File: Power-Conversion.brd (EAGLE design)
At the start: 170.2 x 81 mm, 109 parts, among them T3 FDN340P, U1 ATMEGA328P_TQFP, U4 PCA9685, U5 FT232RLSSOP, U7 LM2678

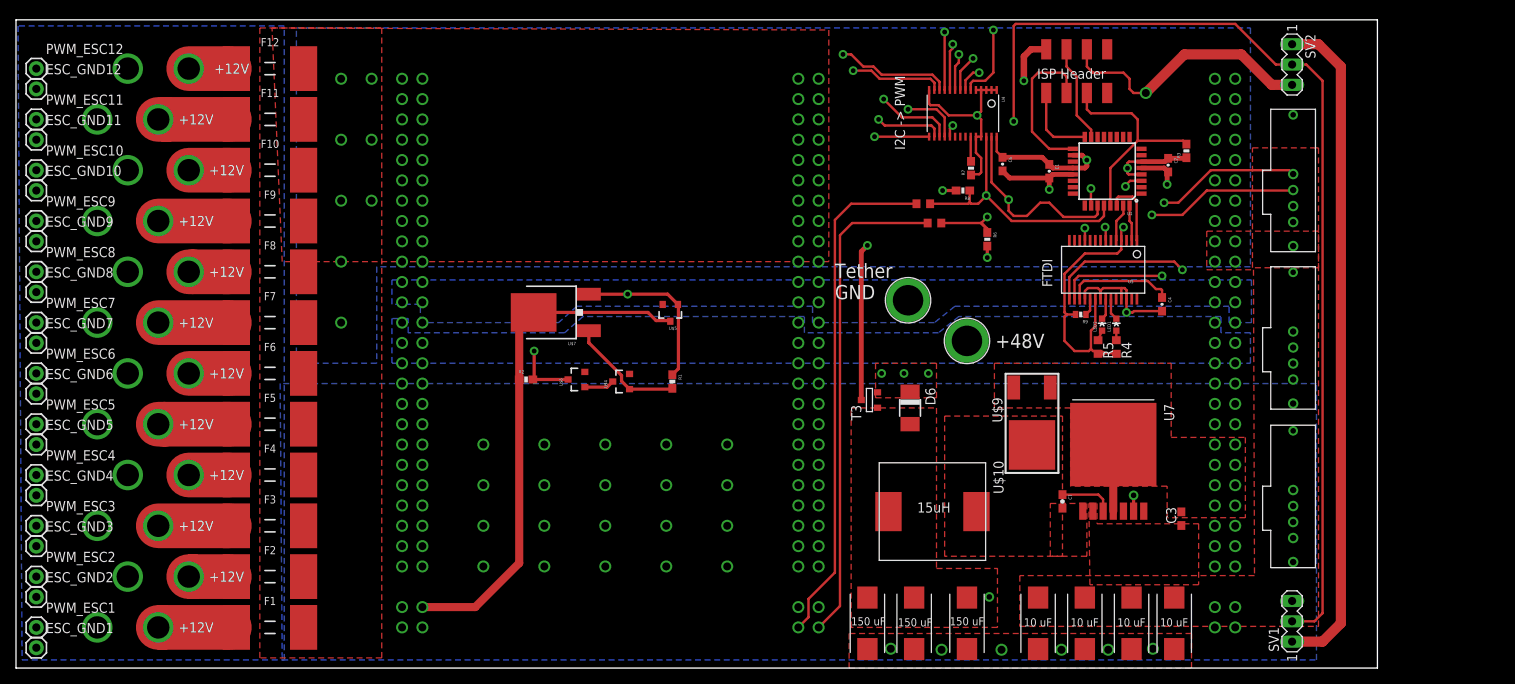
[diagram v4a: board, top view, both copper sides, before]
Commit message: Added debugging pins and more silk screen
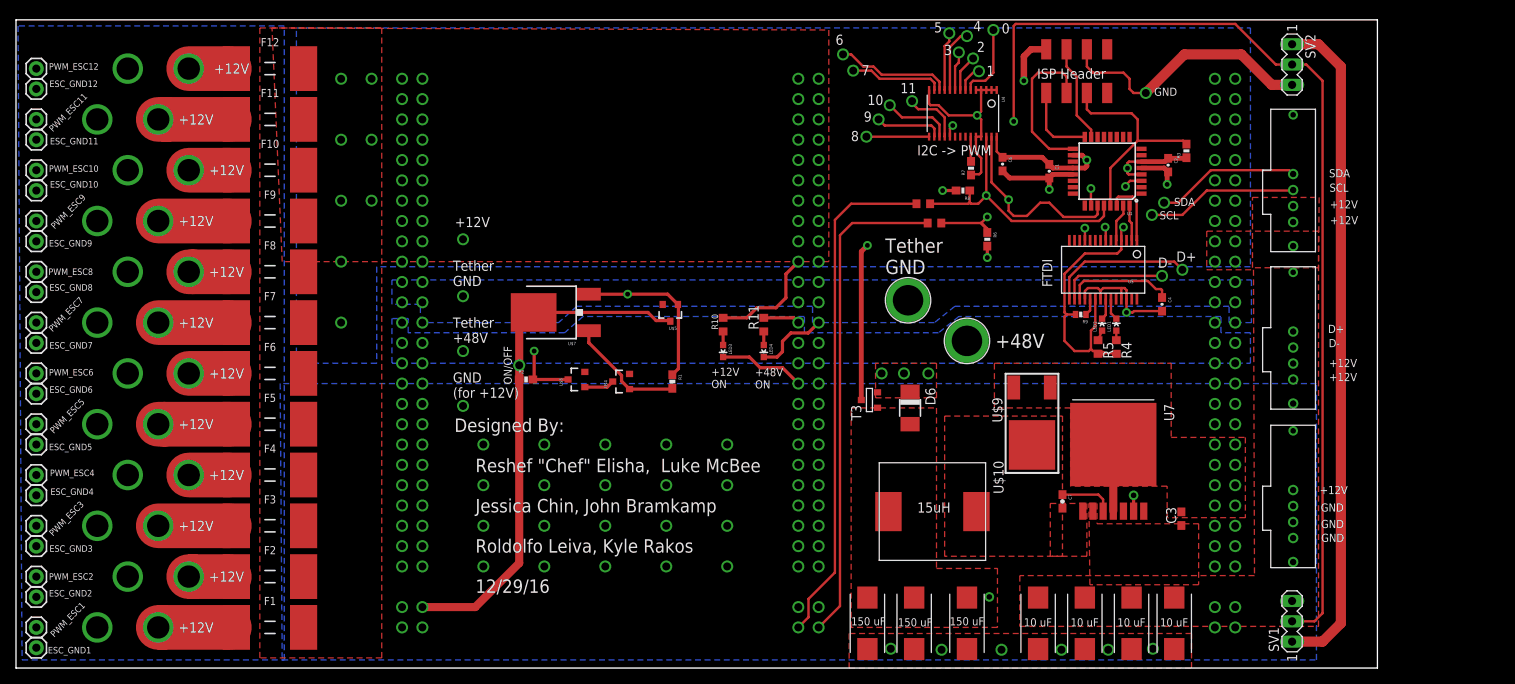
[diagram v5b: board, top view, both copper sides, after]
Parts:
- added LED3: Red, SparkFun:LED-0603
- added LED4: Green, SparkFun:LED-0603
- added R10, R11: 470, resistor:R0603
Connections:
- new net N$39: LED3.A, R10.1
- new net N$40: LED4.A, R11.1
- net GND: now also LED3.C
- net V+: now also R11.2
- net V-: now also LED4.C
- net VCC: now also R10.2
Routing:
- net VCC: track 0.00 -> 14.0 mm
- net GND: track 102.4 -> 113.2 mm
- net V-: track 20.8 -> 30.2 mm, vias 1 -> 2
- net V+: track 8.02 -> 12.6 mm, vias 1 -> 2
- net N$19: track 167.8 -> 172.0 mm
- net N$40: track 0.00 -> 1.70 mm
- net N$39: track 0.00 -> 1.70 mm
- net N$20: track 162.1 -> 162.8 mm
- net N$23: track 144.2 -> 144.8 mm
- net ONOFF: track 167.7 -> 167.9 mm, vias 0 -> 1
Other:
- board text added: "+12V ON"
- board text added: "+48V ON"
- board text added: "0"
- board text added: "1"
- board text added: "10"
- board text added: "11"
- board text added: "2"
- board text added: "3"
- board text added: "4"
- board text added: "5"
- board text added: "6"
- board text added: "7"
- board text added: "8"
- board text added: "9"
- board text added: "D+"
- board text added: "D-"
- board text added: "Designed By: Reshef "Chef" Elisha, Luke McBee Jessica Chin, John Bramkamp Roldolfo Leiva, Kyle Rakos 12/29/16"
- board text added: "GND"
- board text added: "GND (for +12V)"
- board text added: "ON/OFF"
- board text added: "SCL"
- board text added: "SDA"
- board text added: "Tether +48V"

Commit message: Fixed problem with gnd via
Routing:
- net GND: vias 33 -> 34
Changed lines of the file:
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@@
 <wire x1="93.0148" y1="37.5412" x2="95.8088" y2="37.5412" width="0.4064" layer="1"/>
 <wire x1="95.8088" y1="37.5412" x2="97.79" y2="35.56" width="0.4064" layer="1"/>
+<via x="55.88" y="32.766" extent="1-16" drill="1"/>
 </signal>
 <signal name="SCL">
@@
 <wire x1="93.472" y1="42.076" x2="93.472" y2="40.374" width="0.4064" layer="1"/>
 </signal>
-<signal name="N$41">
-<via x="55.88" y="32.766" extent="1-16" drill="1"/>
-</signal>
 <signal name="N$42">

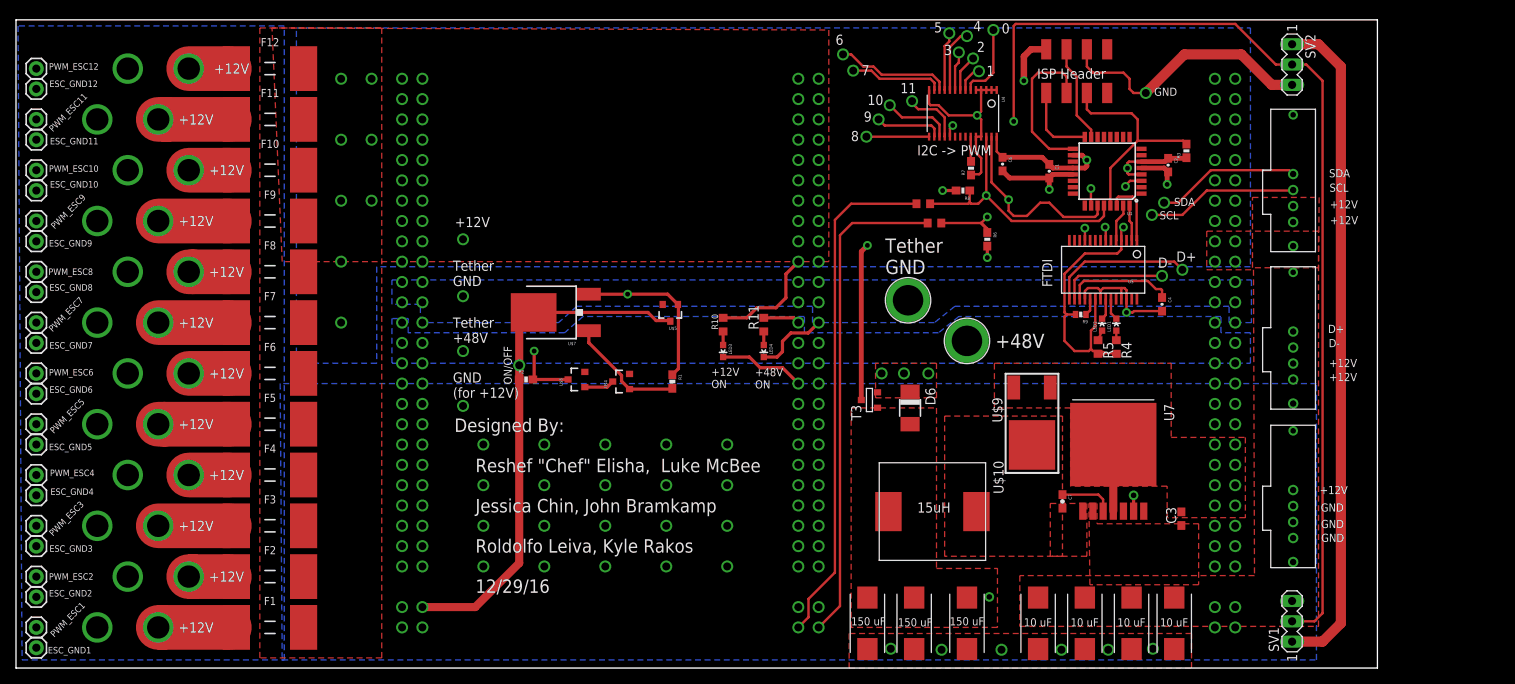
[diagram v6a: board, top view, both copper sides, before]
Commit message: Fixed a few silkscrean problems
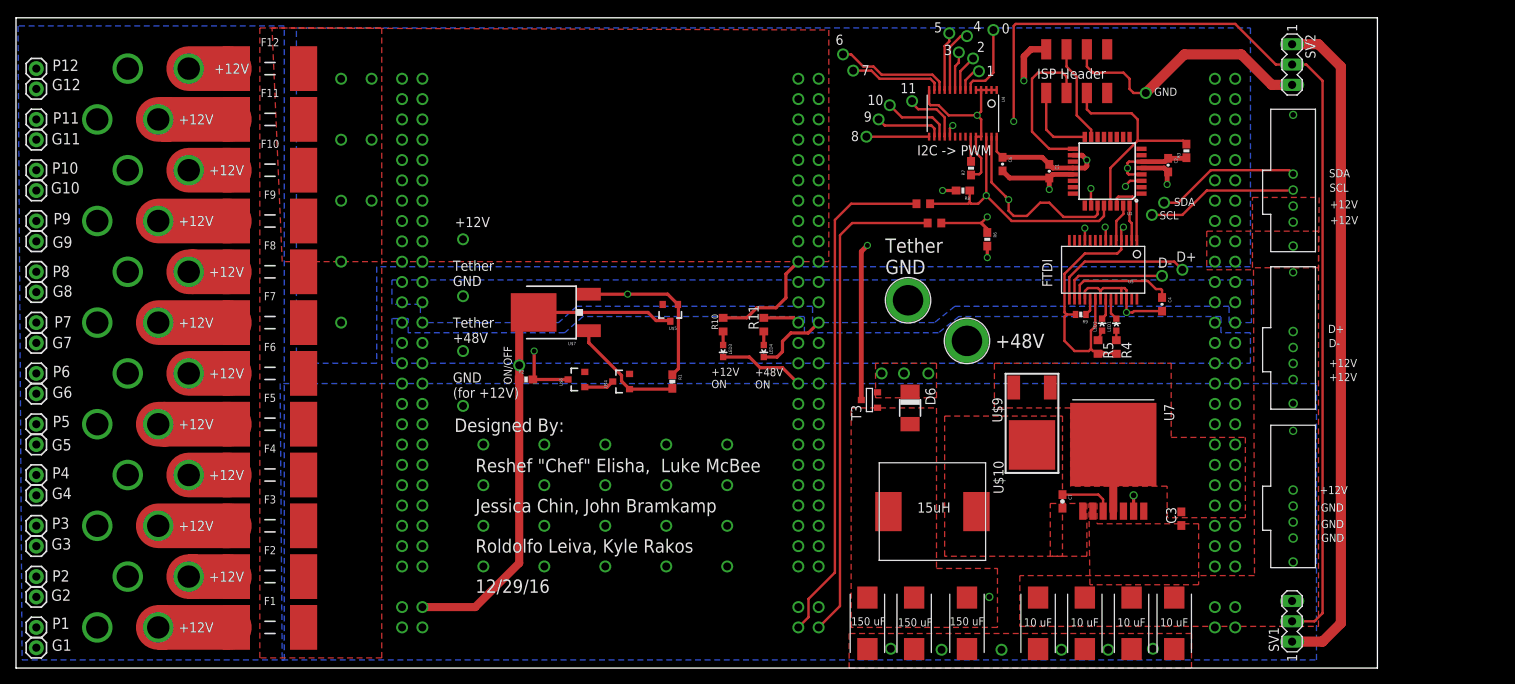
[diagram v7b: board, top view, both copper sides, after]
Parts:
- renumbered ESC_GND1 to G1, ESC_GND10 to G10, ESC_GND11 to G11, ESC_GND12 to G12, ESC_GND2 to G2, ESC_GND3 to G3, ESC_GND4 to G4, ESC_GND5 to G5, ESC_GND6 to G6, ESC_GND7 to G7, ESC_GND8 to G8, ESC_GND9 to G9, PWM_ESC1 to P1, PWM_ESC10 to P10, PWM_ESC11 to P11, PWM_ESC12 to P12, PWM_ESC2 to P2, PWM_ESC3 to P3, PWM_ESC4 to P4, PWM_ESC5 to P5, PWM_ESC6 to P6, PWM_ESC7 to P7, PWM_ESC8 to P8, PWM_ESC9 to P9
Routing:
- net VCC: vias 8 -> 9
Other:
- board size 170.2 x 81 mm -> 170.2 x 81.3 mm

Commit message: stuff
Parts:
- added LED5, LED6: Red, SparkFun:LED-0603
- added R12, R13: 470, resistor:R0603
- added RN1, RN2: (no value), resistor-dil:0603-ARC
- moved C11 1.51 mm to (127.8, 7.10)
- moved C12 1.51 mm to (139.4, 7.10)
- moved C13 1.51 mm to (133.6, 7.10)
- moved C14 1.51 mm to (144.8, 7.10)
- moved C10 1.00 mm to (118.9, 6.59)
- moved C8 1.00 mm to (106.4, 6.59)
- moved C9 1.00 mm to (112.3, 6.59)
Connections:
- new net A0: RN1.1, U4.1
- new net A1: RN1.2, U4.2
- new net A2: RN1.3, U4.3
- new net A3: RN1.4, U4.4
- new net A4: RN2.1, U4.5
- new net A5: RN2.2, U4.24
- new net LED1: R12.2, U1.1
- new net LED2: R13.2, U1.2
- new net N$41: LED5.A, R12.1
- new net N$42: LED6.A, R13.1
- net GND: now also LED5.C, LED6.C, RN1.5, RN1.6, RN1.7, RN1.8, RN2.5, RN2.6, RN2.7, RN2.8; no longer U4.1, U4.2, U4.24, U4.3, U4.4, U4.5
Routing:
- net GND: track 113.2 -> 126.4 mm, vias 34 -> 35
- net A5: track 0.00 -> 9.74 mm
- net LED1: track 0.00 -> 8.71 mm
- net LED2: track 0.00 -> 7.86 mm
- net A4: track 0.00 -> 7.28 mm
- net A3: track 0.00 -> 6.14 mm
- net A2: track 0.00 -> 5.10 mm
- net A1: track 0.00 -> 4.05 mm
- net N$31: track 19.5 -> 16.0 mm
- net A0: track 0.00 -> 3.04 mm
- net N$42: track 0.00 -> 1.70 mm
- net N$41: track 0.00 -> 1.70 mm
- net N$29: track 9.77 -> 8.08 mm
- net +5V_USB: track 58.5 -> 59.6 mm
- net PWM13: vias 2 -> 1
